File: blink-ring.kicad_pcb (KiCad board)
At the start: 2 copper layers, 18.6 x 18.6 mm, 35 parts, among them SW1 SW_SPDT, U1 ATtiny85_QFN20_1-5, U2 ATtiny85_QFN20_11-15

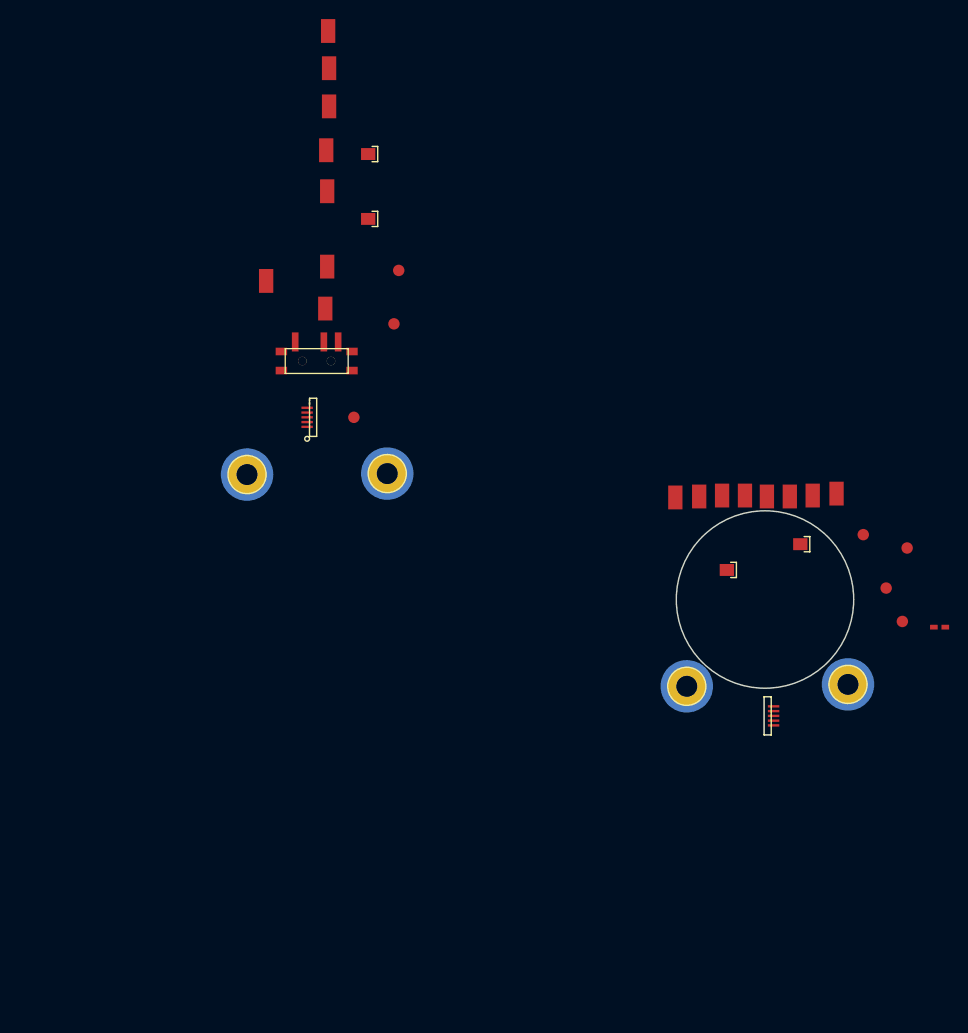
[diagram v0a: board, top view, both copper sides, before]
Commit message: finalized PCB outline and layout. ordered first rev.
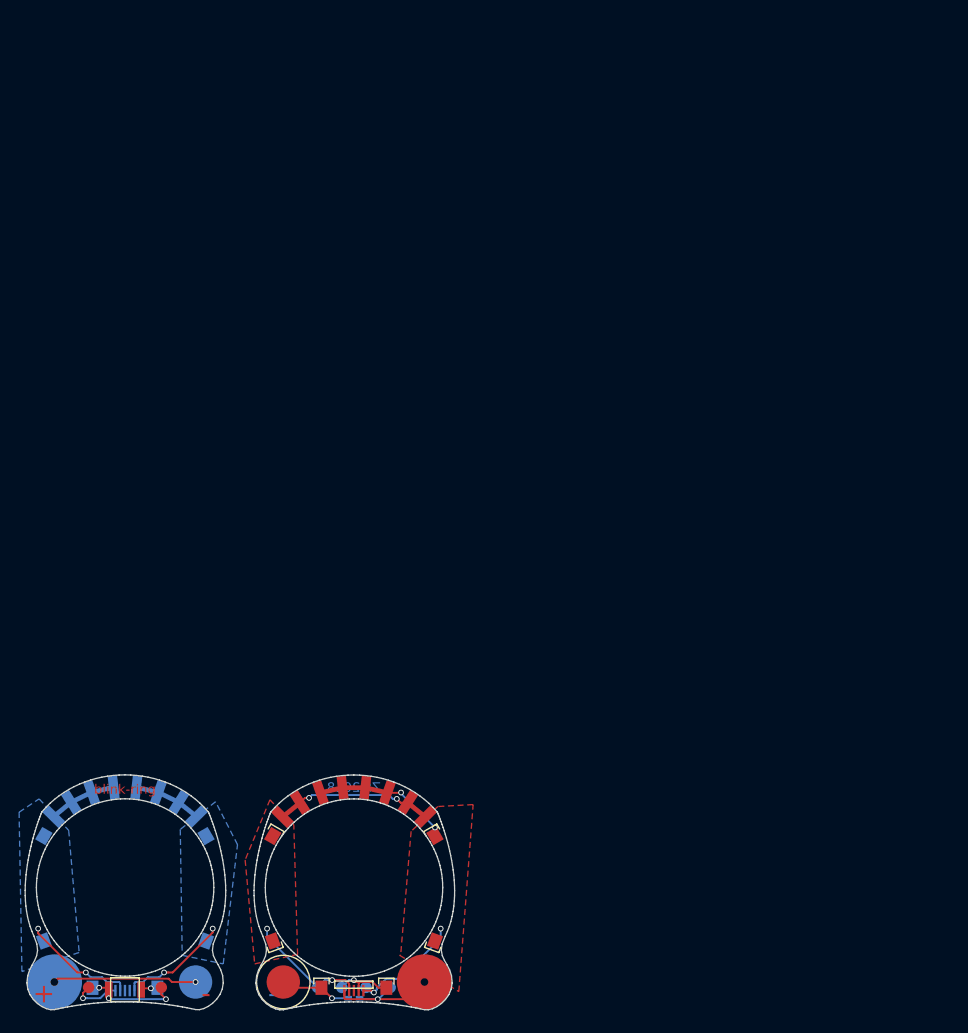
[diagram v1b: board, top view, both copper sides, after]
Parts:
- removed TP6: GND, KiCad_Footprints:ZF_CONN_1-2_pad
- added REF**: ZF_SMD_0805_CORD, KiCad_Footprints:ZF_SMD_0805_CORD, F.Cu at (98.5, 134.5)
- added REF**: ZF_SMD_0805_CORD, KiCad_Footprints:ZF_SMD_0805_CORD, F.Cu at (98.5, 145.5)
- added REF**: ZF_SMD_0805_CORD, KiCad_Footprints:ZF_SMD_0805_CORD, B.Cu at (74.5, 145.5)
- added REF**: ZF_SMD_0805_CORD, KiCad_Footprints:ZF_SMD_0805_CORD, B.Cu at (57.5, 145.5)
- added REF**: ZF_SMD_0805_CORD, KiCad_Footprints:ZF_SMD_0805_CORD, F.Cu at (81.5, 145.5)
- added REF**: ZF_SMD_0805_CORD, KiCad_Footprints:ZF_SMD_0805_CORD, B.Cu at (57.5, 134.5)
- added REF**: ZF_SMD_0805_CORD, KiCad_Footprints:ZF_SMD_0805_CORD, B.Cu at (74.5, 134.5)
- added REF**: ZF_SMD_0805_CORD, KiCad_Footprints:ZF_SMD_0805_CORD, F.Cu at (81.5, 134.5)
- C1, NA3, TP2, TP3, TP4, TP5, U1: moved to B.Cu
- D1: value LED0 -> ZF_SMD_0805_CORD; moved to B.Cu
- D2: value LED1 -> ZF_SMD_0805_CORD
- D3: value LED2 -> ZF_SMD_0805_CORD; moved to B.Cu
- D4: value LED3 -> ZF_SMD_0805_CORD
- D5: value LED4 -> ZF_SMD_0805_CORD; moved to B.Cu
- D6: value LED5 -> ZF_SMD_0805_CORD
- D7: value LED6 -> ZF_SMD_0805_CORD; moved to B.Cu
- D8: value LED7 -> ZF_SMD_0805_CORD
- NA1: value RST_PULLUP -> SW_JMP; moved to B.Cu
- NA2: value RST_PULLUP -> SW_JMP
- R1: footprint KiCad_Footprints:ZF_STRUCT_2-2_HOLE -> KiCad_Footprints:ZF_BATT_AC10E_NEG; moved to B.Cu
- R10: value LED5 -> ZF_SMD_0805_CORD; moved to B.Cu
- R11: value LED6 -> ZF_SMD_0805_CORD
- R12: value LED7 -> ZF_SMD_0805_CORD; moved to B.Cu
- R2: footprint KiCad_Footprints:ZF_STRUCT_2-2_HOLE -> KiCad_Footprints:ZF_BATT_AC10E_POS
- R3: footprint KiCad_Footprints:ZF_STRUCT_2-2_HOLE -> KiCad_Footprints:ZF_BATT_AC10E_POS; moved to B.Cu
- R4: footprint KiCad_Footprints:ZF_STRUCT_2-2_HOLE -> KiCad_Footprints:ZF_BATT_AC10E_NEG
- R5: value LED0 -> ZF_SMD_0805_CORD
- R6: value LED1 -> ZF_SMD_0805_CORD; moved to B.Cu
- R7: value LED2 -> ZF_SMD_0805_CORD
- R8: value LED3 -> ZF_SMD_0805_CORD; moved to B.Cu
- R9: value LED4 -> ZF_SMD_0805_CORD
- SW1: value SW_SPDT -> SW_PUSH; footprint KiCad_Footprints:ZF_SW_PCM12SMTR -> KiCad_Footprints:ZF_SW_B3U
- moved NA1 90.2 mm to (69.4, 150.4), turned to 90 degrees
- moved D1 87.2 mm to (58.5, 132.5), turned to 45.5 degrees
- moved NA3 85.6 mm to (62.6, 150.4), turned to 90 degrees
- moved TP1 81.9 mm to (62.2, 150.4)
- moved R6 81.6 mm to (60.4, 131.0), turned to 32.5 degrees
- moved D5 74.2 mm to (67.2, 129.4), turned to 353.5 degrees
- moved TP7 73.7 mm to (69.8, 150.4)
- moved C1 72.7 mm to (90.0, 151.5), turned to 180 degrees
- moved TP5 71.1 mm to (93.8, 150.4)
- moved TP3 70.8 mm to (88.7, 150.4)
- moved R10 69.6 mm to (69.5, 129.9), turned to 340.5 degrees
- moved SW1 68.9 mm to (66.0, 150.6)
- moved NA4 68.4 mm to (86.6, 150.4), turned to 90 degrees
- moved TP4 68.1 mm to (91.3, 150.4)
- moved R12 67.0 mm to (73.5, 132.5), turned to 314.5 degrees
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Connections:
- NA2 pad 1: VCC -> Net-(NA2-Pad1)
- R3 pad 1: Net-(R3-Pad1) -> Net-(R1-Pad1)
- SW1 pad 1: Net-(R3-Pad1) -> Net-(NA3-Pad1)
- SW1 pad 2: Net-(R1-Pad1) -> Net-(NA1-Pad1)
- TP1 pad 1: Net-(NA1-Pad1) -> Net-(TP1-Pad1)
- TP3 pad 1: Net-(TP3-Pad1) -> Net-(NA2-Pad1)
- U1 pad 1: Net-(NA1-Pad1) -> Net-(TP1-Pad1)
- U2 pad 12: Net-(TP3-Pad1) -> Net-(NA2-Pad1)
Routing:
- net /LED_TOP_0: track 0.00 -> 29.6 mm, vias 0 -> 4
- net /LED_TOP_1: track 0.00 -> 26.4 mm, vias 0 -> 4
- net /LED_BOTTOM_0: track 0.00 -> 19.2 mm, vias 0 -> 2
- net /LED_BOTTOM_1: track 0.00 -> 18.7 mm, vias 0 -> 2
- net Net-(R1-Pad1): track 0.00 -> 15.1 mm, vias 0 -> 1
- net VCC: track 0.00 -> 13.7 mm, vias 0 -> 1
- net Net-(NA3-Pad1): track 0.00 -> 10.2 mm, vias 0 -> 3
- net GND: track 0.00 -> 7.50 mm, vias 0 -> 1
- net Net-(NA2-Pad1): track 0.00 -> 6.26 mm, vias 0 -> 1
- net Net-(TP1-Pad1): track 0.00 -> 5.11 mm, vias 0 -> 1
- net Net-(NA1-Pad1): track 0.00 -> 1.78 mm, vias 0 -> 1
- added copper zone on B.Cu, net /LED_BOTTOM_0
- added copper zone on B.Cu, net /LED_BOTTOM_1
- added copper zone on F.Cu, net /LED_TOP_0
- added copper zone on F.Cu, net /LED_TOP_1
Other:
- board size 18.6 x 18.6 mm -> 45 x 24.6 mm
- net class Default: trace_width 0.25 -> 0.2
- rule pad_to_mask_clearance: 0.2 -> 0
- board text added: "+"
- board text added: "-"
- board text added: "BOTTOM"
- board text added: "TOP"
- board text added: "ZF 2018"
- board text added: "blink-ring"
- board text added: "radius = 10.5mm count = 8 degrees = 13"

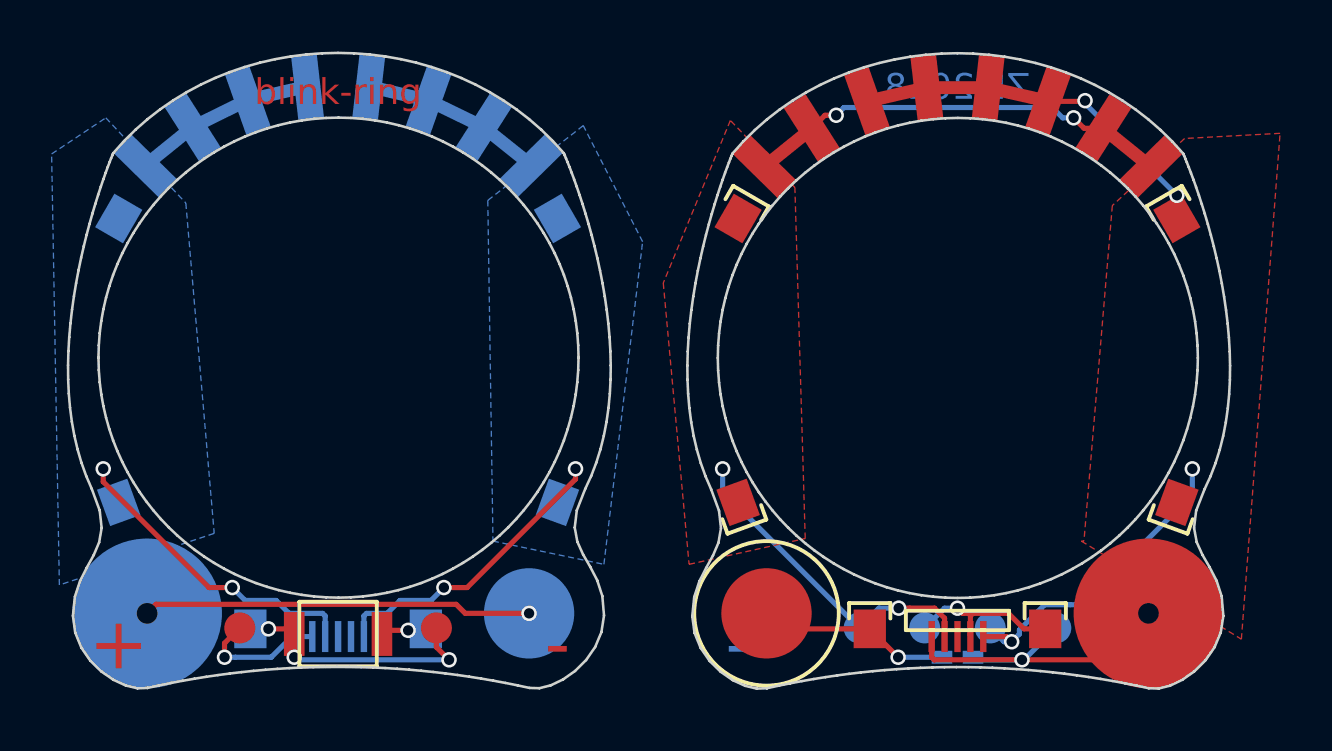
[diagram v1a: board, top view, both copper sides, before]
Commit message: new PCB rev. added reinforcements, changed battery contact, fixed open LED trace
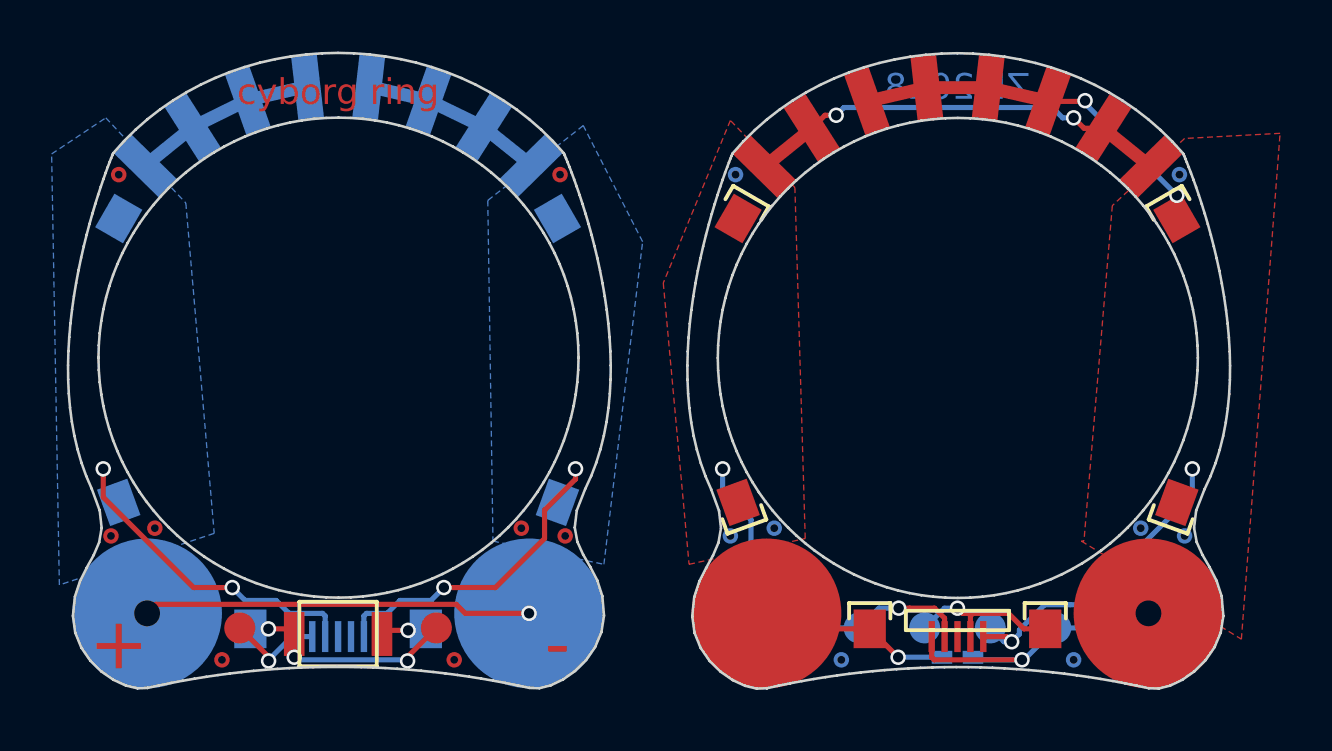
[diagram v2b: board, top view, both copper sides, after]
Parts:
- added REF**: ZF_STRUCT_HOLE_0-30mm, KiCad_Footprints:ZF_STRUCT_HOLE_0-30mm, B.Cu at (98.6, 132.8)
- added REF**: ZF_STRUCT_HOLE_0-30mm, KiCad_Footprints:ZF_STRUCT_HOLE_0-30mm, F.Cu at (57.2, 146.8)
- added REF**: ZF_STRUCT_HOLE_0-30mm, KiCad_Footprints:ZF_STRUCT_HOLE_0-30mm, F.Cu at (58.9, 146.5)
- added REF**: ZF_STRUCT_HOLE_0-30mm, KiCad_Footprints:ZF_STRUCT_HOLE_0-30mm, F.Cu at (73.1, 146.5)
- added REF**: ZF_STRUCT_HOLE_0-30mm, KiCad_Footprints:ZF_STRUCT_HOLE_0-30mm, F.Cu at (74.8, 146.8)
- added REF**: ZF_STRUCT_HOLE_0-30mm, KiCad_Footprints:ZF_STRUCT_HOLE_0-30mm, B.Cu at (81.2, 146.8)
- added REF**: ZF_STRUCT_HOLE_0-30mm, KiCad_Footprints:ZF_STRUCT_HOLE_0-30mm, B.Cu at (82.9, 146.5)
- added REF**: ZF_STRUCT_HOLE_0-30mm, KiCad_Footprints:ZF_STRUCT_HOLE_0-30mm, B.Cu at (98.8, 146.8)
- added REF**: ZF_STRUCT_HOLE_0-30mm, KiCad_Footprints:ZF_STRUCT_HOLE_0-30mm, B.Cu at (97.1, 146.5)
- added REF**: ZF_STRUCT_HOLE_0-30mm, KiCad_Footprints:ZF_STRUCT_HOLE_0-30mm, F.Cu at (57.5, 132.8)
- added REF**: ZF_STRUCT_HOLE_0-30mm, KiCad_Footprints:ZF_STRUCT_HOLE_0-30mm, F.Cu at (74.6, 132.8)
- added REF**: ZF_STRUCT_HOLE_0-30mm, KiCad_Footprints:ZF_STRUCT_HOLE_0-30mm, B.Cu at (81.4, 132.8)
- added REF**: ZF_STRUCT_HOLE_0-30mm, KiCad_Footprints:ZF_STRUCT_HOLE_0-30mm, F.Cu at (61.5, 151.6)
- added REF**: ZF_STRUCT_HOLE_0-30mm, KiCad_Footprints:ZF_STRUCT_HOLE_0-30mm, F.Cu at (70.5, 151.6)
- added REF**: ZF_STRUCT_HOLE_0-30mm, KiCad_Footprints:ZF_STRUCT_HOLE_0-30mm, B.Cu at (85.5, 151.6)
- added REF**: ZF_STRUCT_HOLE_0-30mm, KiCad_Footprints:ZF_STRUCT_HOLE_0-30mm, B.Cu at (94.5, 151.6)
- D1, R5: value ZF_SMD_0805_CORD -> LED0
- D2, R6: value ZF_SMD_0805_CORD -> LED1
- D3, R7: value ZF_SMD_0805_CORD -> LED2
- D4, R8: value ZF_SMD_0805_CORD -> LED3
- D5, R9: value ZF_SMD_0805_CORD -> LED4
- D6, R10: value ZF_SMD_0805_CORD -> LED5
- D7, R11: value ZF_SMD_0805_CORD -> LED6
- D8, R12: value ZF_SMD_0805_CORD -> LED7
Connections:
- REF** pad 1: /LED_TOP_0 -> /LED_TOP_1
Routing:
- net VCC: track 13.7 -> 11.9 mm
- net Net-(NA3-Pad1): track 10.2 -> 8.88 mm
- net Net-(TP1-Pad1): track 5.11 -> 3.85 mm
- net /LED_TOP_1: track 26.4 -> 27.3 mm
- net /LED_BOTTOM_1: track 18.7 -> 19.4 mm
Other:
- board text added: "cyborg ring"
- board text removed: "blink-ring"
